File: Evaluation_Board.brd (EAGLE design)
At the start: 60.9 x 39.4 mm, 38 parts, among them IC1 MEGA32-A, IC2 FT232RL, IC3 317EMP, J1 DCJ0202, Q1 16 MHz

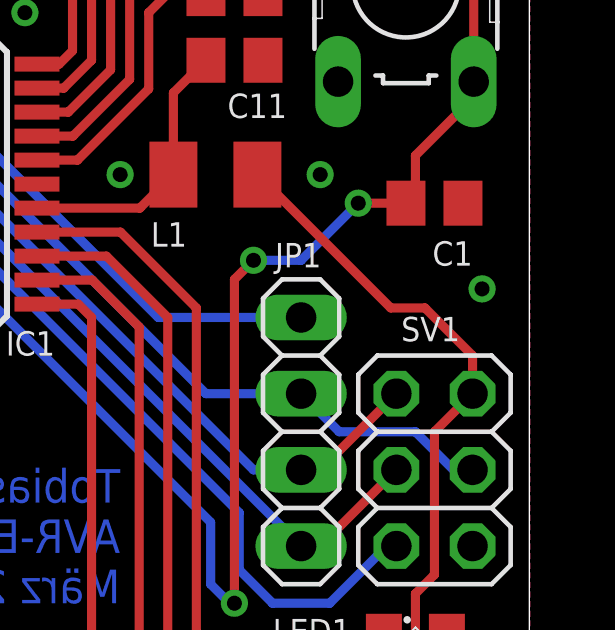
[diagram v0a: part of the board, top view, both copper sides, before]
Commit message: Added name for ISP connector and placed a pin-one-marker on silk screen layer.
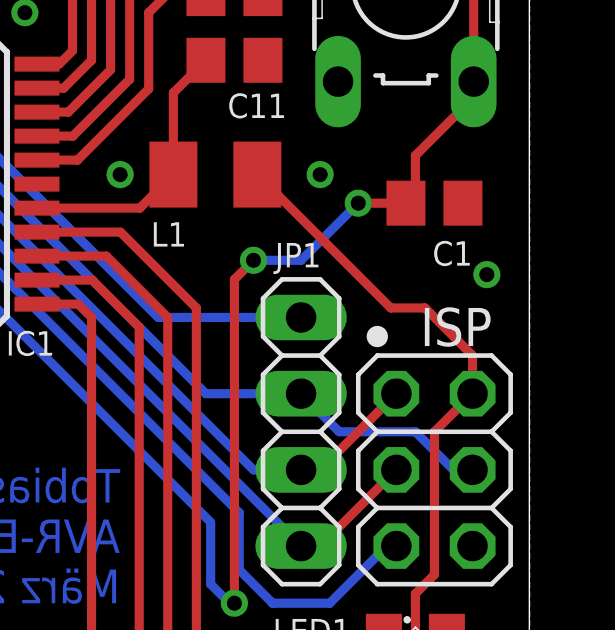
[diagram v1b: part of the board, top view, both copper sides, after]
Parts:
- renumbered SV1 to ISP
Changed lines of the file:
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@@
 AVR-Eval-Board
 März 2015 v1.0</text>
+<circle x="55.88" y="16.51" radius="0.354975" width="0" layer="25"/>
 </plain>
 <attributes>
@@
 <attribute name="MF" value="" x="56.8325" y="11.7475" size="1.778" layer="27" display="off"/>
 <attribute name="OC_FARNELL" value="176432" x="56.8325" y="11.7475" size="1.778" layer="27" display="off"/>
-<attribute name="NAME" x="8.763" y="30.9245" size="1.27" layer="25" ratio="10" rot="R180"/>
+<attribute name="NAME" x="8.763" y="30.9245" size="1.27" layer="25" font="vector" ratio="10" rot="R180"/>
 <attribute name="VALUE" x="2.9845" y="29.5275" size="1.27" layer="27" ratio="10"/>
 </element>
@@
 <attribute name="VALUE" x="-7.3025" y="14.605" size="1.27" layer="27"/>
 </element>
-<element name="SV1" library="pinhead" package="2X03" value="ISP" x="57.785" y="12.065" smashed="yes" rot="R270">
-<attribute name="NAME" x="56.67375" y="16.35125" size="0.8128" layer="25" ratio="10"/>
+<element name="ISP" library="pinhead" package="2X03" value="ISP" x="57.785" y="12.065" smashed="yes" rot="R270">
+<attribute name="NAME" x="57.30875" y="16.1925" size="1.27" layer="25" font="vector" ratio="12"/>
 <attribute name="VALUE" x="53.34" y="15.875" size="1.27" layer="27" rot="R270"/>
 </element>
@@
 </signal>
 <signal name="RESET">
-<contactref element="SV1" pad="5"/>
+<contactref element="ISP" pad="5"/>
 <contactref element="R1" pad="1"/>
 <contactref element="IC1" pad="4"/>
@@
 </signal>
 <signal name="SCK">
-<contactref element="SV1" pad="3"/>
+<contactref element="ISP" pad="3"/>
 <contactref element="IC1" pad="3"/>
 <contactref element="JP1" pad="1"/>
@@
 </signal>
 <signal name="MISO">
-<contactref element="SV1" pad="1"/>
+<contactref element="ISP" pad="1"/>
 <contactref element="JP1" pad="2"/>
 <contactref element="IC1" pad="2"/>
@@
 </signal>
 <signal name="MOSI">
-<contactref element="SV1" pad="4"/>
+<contactref element="ISP" pad="4"/>
 <contactref element="IC1" pad="1"/>
 <contactref element="JP1" pad="3"/>
@@
 </signal>
 <signal name="GND">
-<contactref element="SV1" pad="6"/>
+<contactref element="ISP" pad="6"/>
 <contactref element="IC2" pad="25"/>
 <contactref element="IC2" pad="21"/>
@@
 <via x="44.45" y="33.9725" extent="1-16" drill="0.5"/>
 <via x="50.165" y="34.29" extent="1-16" drill="0.5"/>
-<via x="59.3725" y="18.0975" extent="1-16" drill="0.5"/>
+<via x="59.53125" y="18.57375" extent="1-16" drill="0.5"/>
 <via x="59.69" y="2.54" extent="1-16" drill="0.5"/>
 <via x="59.69" y="1.27" extent="1-16" drill="0.5"/>
@@
 </signal>
 <signal name="+5V">
-<contactref element="SV1" pad="2"/>
+<contactref element="ISP" pad="2"/>
 <contactref element="LED2" pad="A"/>
 <contactref element="LED3" pad="A"/>
